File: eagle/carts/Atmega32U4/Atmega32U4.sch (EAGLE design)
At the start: 30 parts, among them J6 USB4110-GF-A_REVB, U1 3.3V, U3 32U4, X3 16MHz

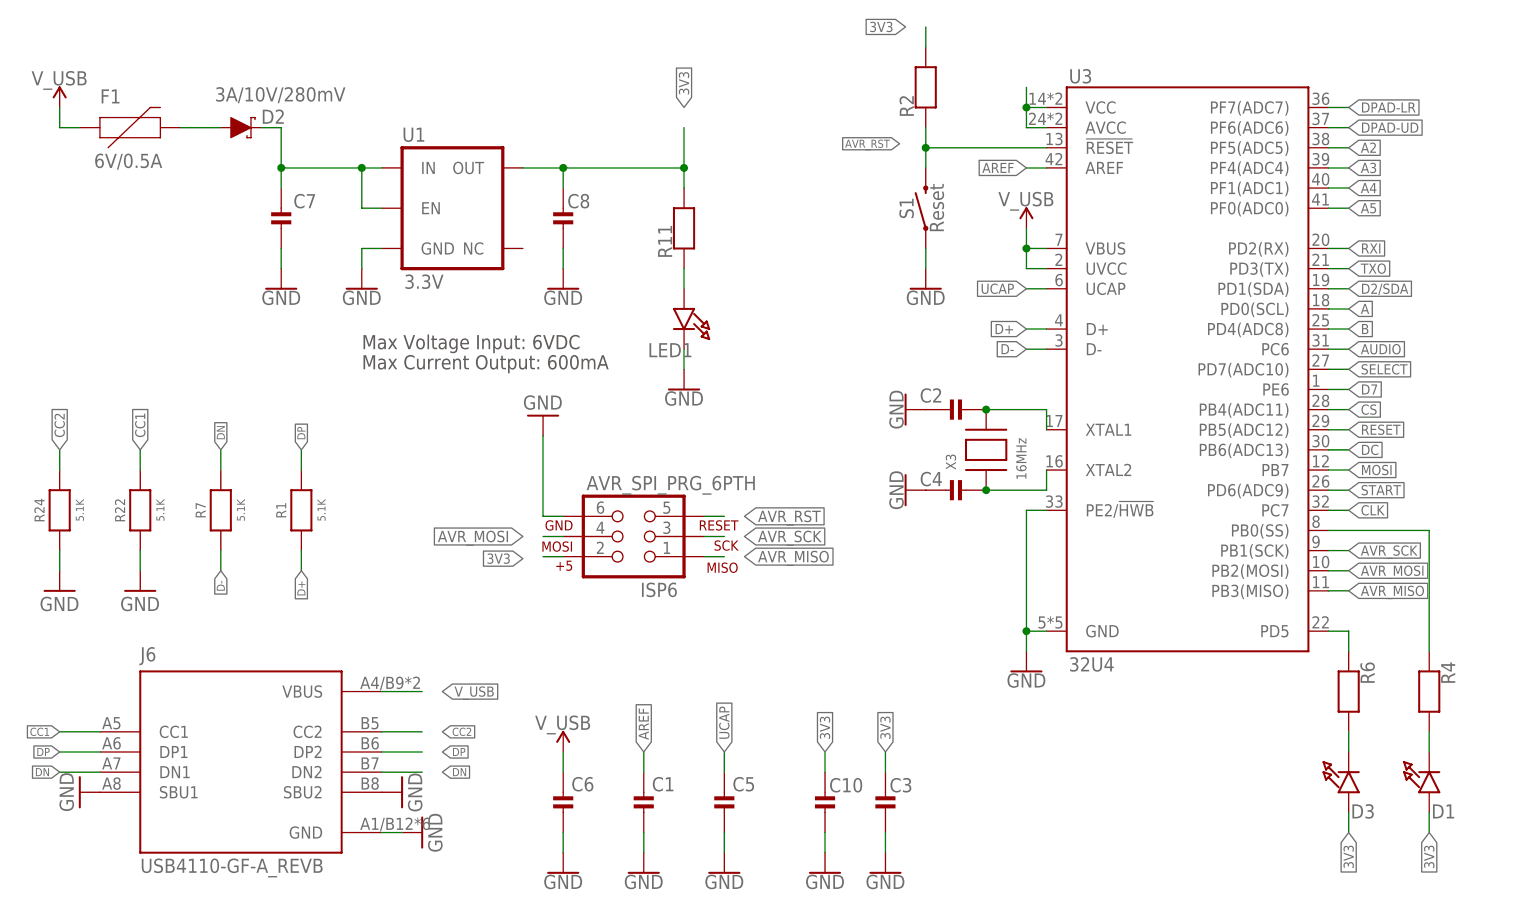
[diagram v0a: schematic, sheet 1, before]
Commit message: feat: update Atmega32u4
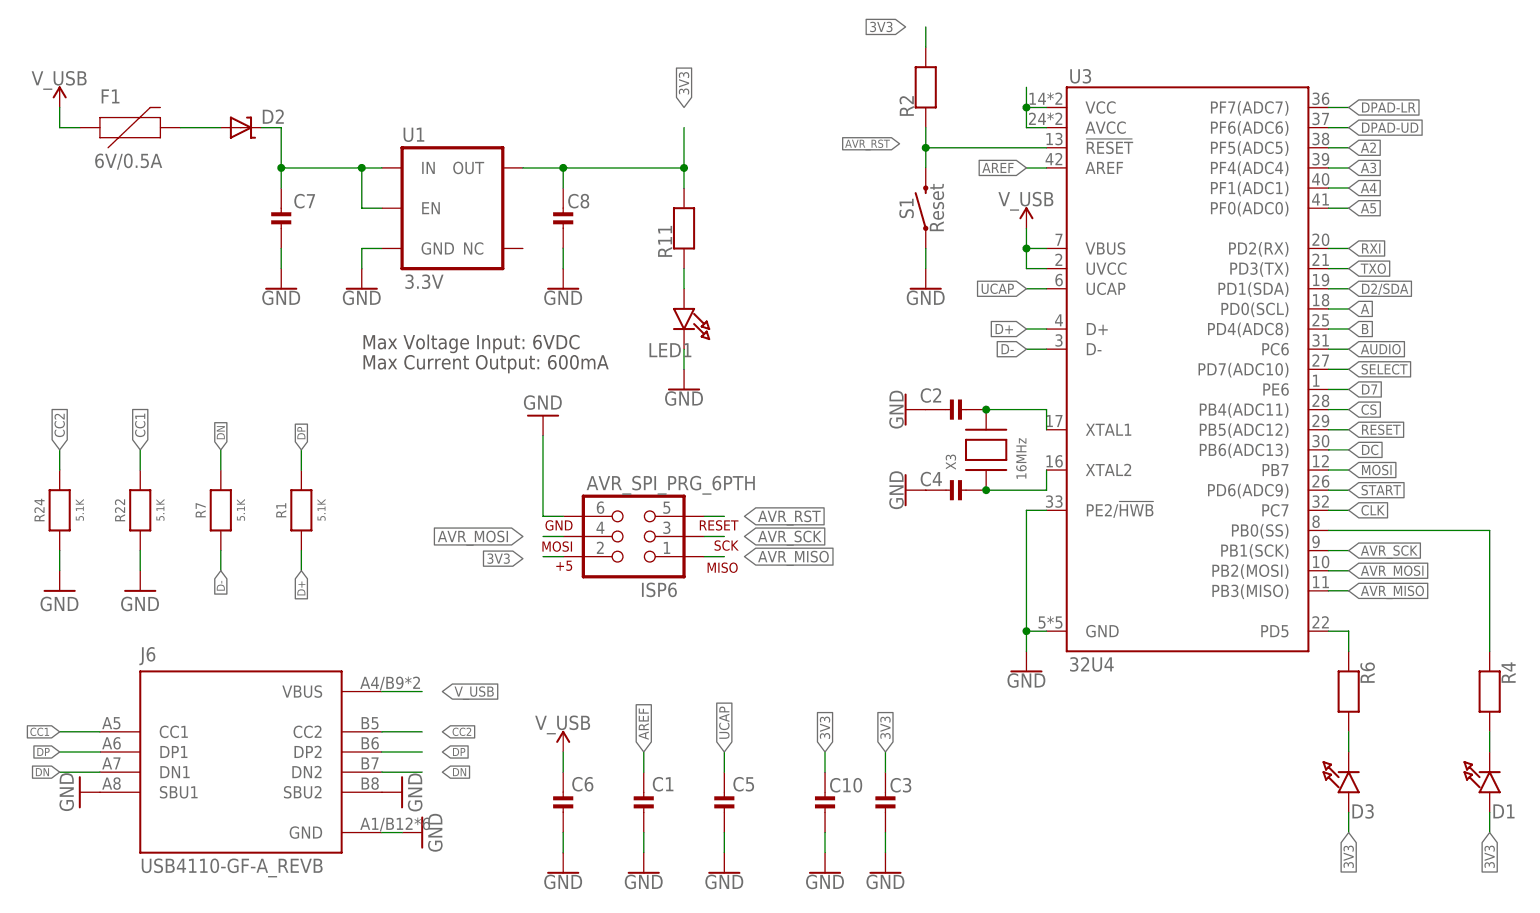
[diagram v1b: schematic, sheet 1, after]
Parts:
- D2: device SparkFun-DiscreteSemi:DIODE-SCHOTTKY-BAT60A -> RetroESP32:DIODE-SCHOTTKYSOD-123; MPN (none) -> MBR120LSFT1G
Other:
- moved on the sheet: D1, R4
